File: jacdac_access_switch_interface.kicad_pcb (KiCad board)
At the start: 2 copper layers, 25 x 35 mm, 26 parts, among them J1 Conn_Jacdac_CardEdge, J2 Conn_HackConnect, J3 jack_3.5_pj313d, J4 jack_3.5_pj313d, U1 NCP114ASN330T1G, U2 STM32G031J6M6, U3 AQY282, U4 AQY282

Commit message: Setting up v1.5, combined input-output
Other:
- board text added: "Switch interface v1.5"
- board text removed: "Switch output v1.4"
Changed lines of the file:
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@@
   (paper "A4")
   (title_block
-    (title "Jacdac access switch output")
+    (title "Jacdac access switch interface")
     (date "2022-01-07")
-    (rev "v1.4")
+    (rev "v1.5")
     (comment 3 "Matthew Oppenheim")
     (comment 4 "Licence: Attribution 4.0 International (CC BY 4.0)")
@@
   (gr_rect (start 154.5 67.5) (end 167.5 69)
     (stroke (width 0.05) (type default)) (fill none) (layer "F.CrtYd"))
-  (gr_text "Switch output\nv1.4" (at 162.5 110.5) (layer "B.SilkS")
+  (gr_text "Switch interface\nv1.5" (at 162.5 110.5) (layer "B.SilkS")
     (effects (font (size 1 1) (thickness 0.16)) (justify mirror))
   )

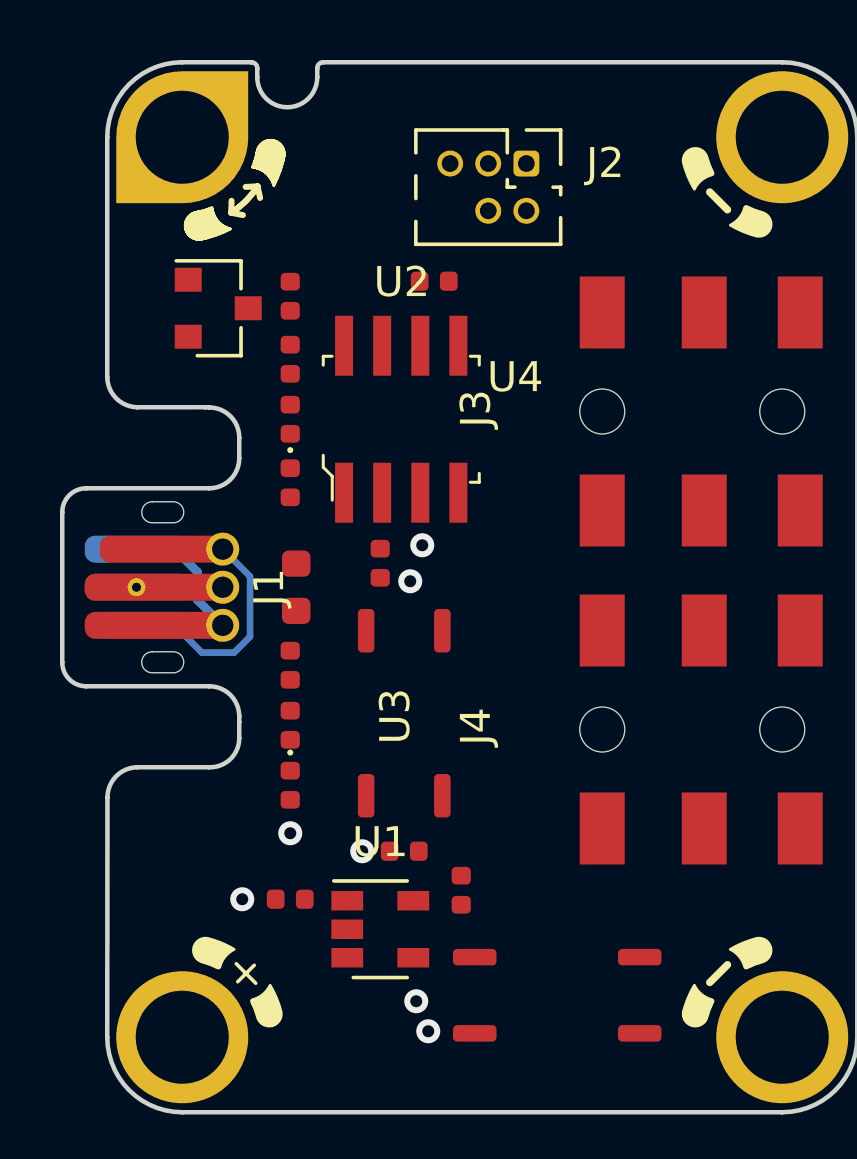
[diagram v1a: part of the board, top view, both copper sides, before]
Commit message: Moving footprint text from silkscreen to user comments
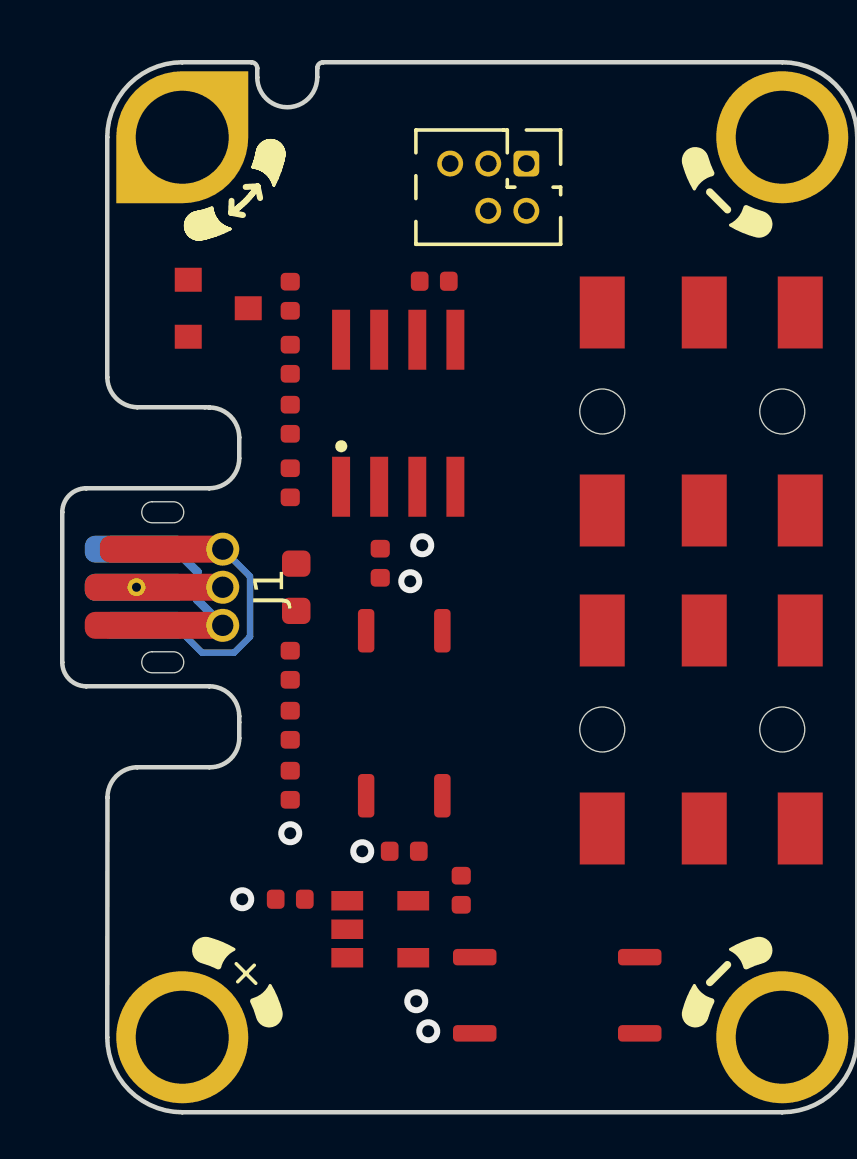
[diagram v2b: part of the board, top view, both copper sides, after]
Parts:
- moved U2 0.22 mm to (157.2, 79.2)

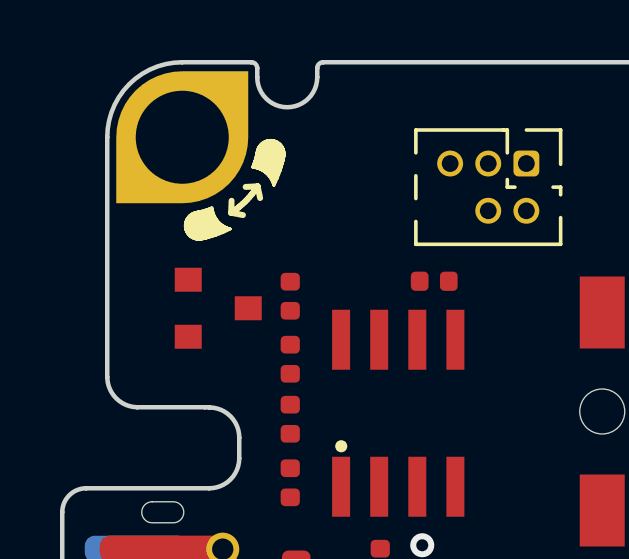
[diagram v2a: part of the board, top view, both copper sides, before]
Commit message: Added input protection. Changed MCU to 20 pin STM32G031F6P6
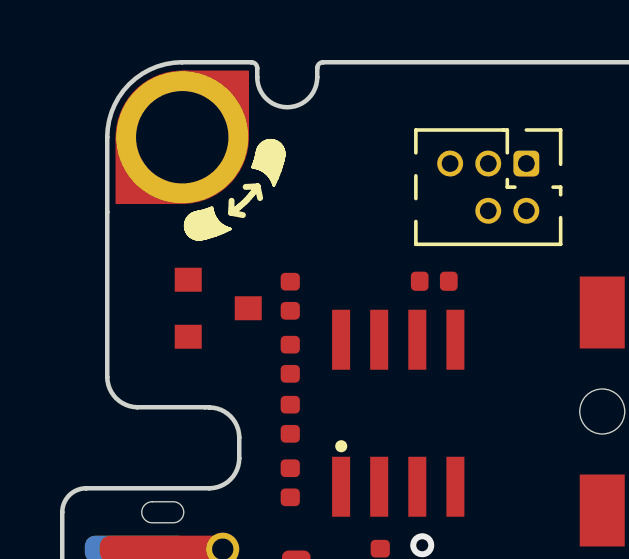
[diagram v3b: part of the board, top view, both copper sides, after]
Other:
- outline, holes or cut-outs redrawn

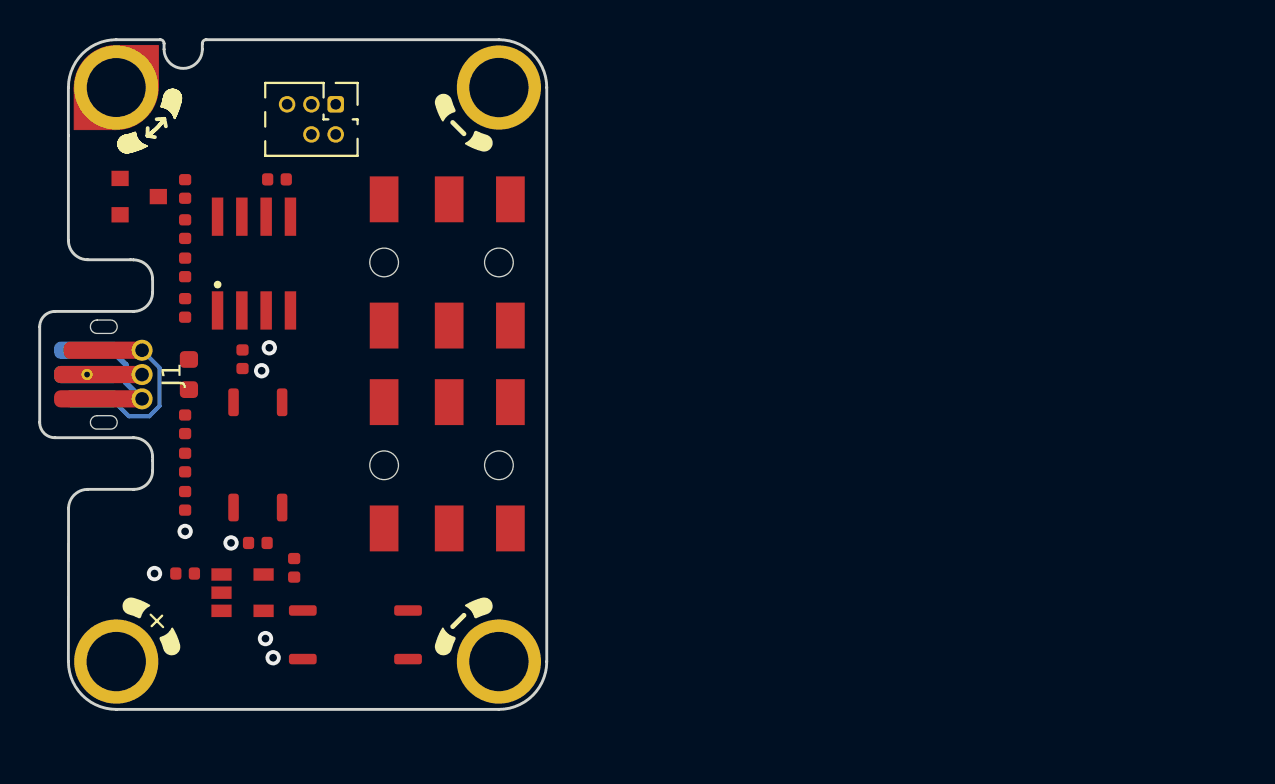
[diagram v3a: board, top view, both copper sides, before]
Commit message: Replaced opto-isoltated relays with discrete FET relays
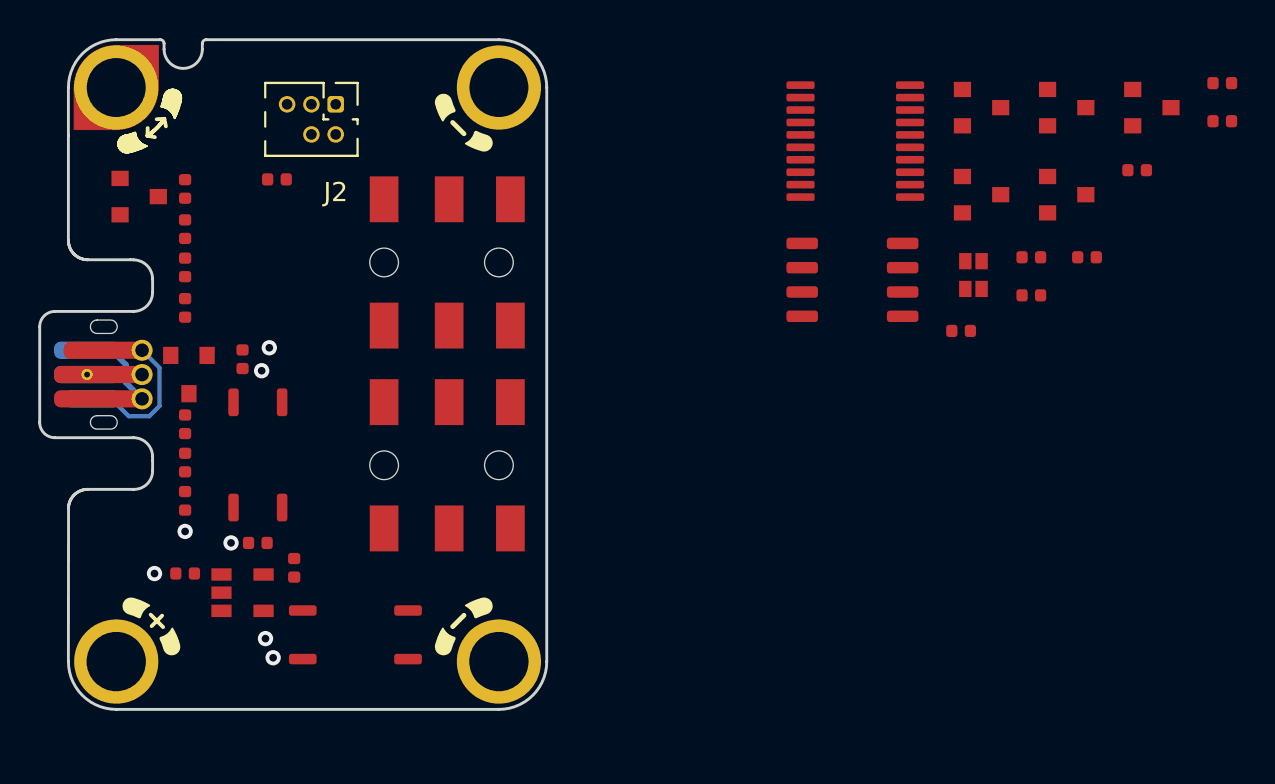
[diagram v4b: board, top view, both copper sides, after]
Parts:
- removed U2: STM32G031J6M6, jacdac_access_switch_interface:SOIC-8_W3.9mm
- added D10: BAT54S, jacdac_access_switch_interface:SOT-23, F.Cu at (199.7, 75.6)
- added D5: LTST-C19HE1WT, jacdac_access_switch_interface:LED_LTST-C19HE1WT, F.Cu at (194.8, 79.8)
- added D6: BAT54S, jacdac_access_switch_interface:SOT-23, F.Cu at (204.1, 71.0)
- added D7: BAT54S, jacdac_access_switch_interface:SOT-23, F.Cu at (199.7, 71.0)
- added D8: BAT54S, jacdac_access_switch_interface:SOT-23, F.Cu at (195.2, 71.0)
- added D9: BAT54S, jacdac_access_switch_interface:SOT-23, F.Cu at (195.2, 75.6)
- added Q1: WSP6946, jacdac_access_switch_interface:SOP-8_3.9x4.9mm_P1.27mm, F.Cu at (188.5, 80.0)
- added R10: 100K, jacdac_access_switch_interface:R_0402_1005Metric, F.Cu at (207.8, 71.8)
- added R11: 100K, jacdac_access_switch_interface:R_0402_1005Metric, F.Cu at (200.7, 78.9)
- added R12: 100K, jacdac_access_switch_interface:R_0402_1005Metric, F.Cu at (194.2, 82.7)
- added R6: 150, jacdac_access_switch_interface:R_0402_1005Metric, F.Cu at (197.8, 80.9)
- added R7: 33, jacdac_access_switch_interface:R_0402_1005Metric, F.Cu at (203.4, 74.3)
- added R8: 33, jacdac_access_switch_interface:R_0402_1005Metric, F.Cu at (207.8, 69.8)
- added R9: 100K, jacdac_access_switch_interface:R_0402_1005Metric, F.Cu at (197.8, 78.9)
- added U5: STM32G031F6P6, jacdac_access_switch_interface:TSSOP-20_4.4x6.5mm_P0.65mm, F.Cu at (188.6, 72.8)
- D4: value LED -> BAT54S; footprint jacdac_access_switch_interface:LED_0603_1608Metric -> jacdac_access_switch_interface:SOT-23
- R4: value 330 -> 100K
- R5: value 220 -> 100K
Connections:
- net /PLUG_TIP1 renamed /TIP1
- net /PLUG_TIP2 renamed /TIP2
- D3 pad 3: /JD_DATA_MCU_SWCLK -> Net-(D3-common)
- D4 pad 1: /JD_STATUS -> GND
- D4 pad 2: Net-(D4-A) -> +3V3
- J2 pad 4: /JD_DATA_MCU_SWCLK -> /SWDCLK
- J3 pad 3: /SLEEVE1 -> /RING1
- J4 pad 3: /SLEEVE2 -> /RING2
- R1 pad 1: /JD_DATA_MCU_SWCLK -> Net-(D3-common)
- R2 pad 2: /SWITCH1 -> /RELAY1
- R3 pad 2: /SWITCH2 -> /RELAY2
- R4 pad 1: +3V3 -> /SLEEVE1_P
- R4 pad 2: Net-(D4-A) -> unconnected-(R4-Pad2)
- R5 pad 1: +3V3 -> /RING1_P
- R5 pad 2: Net-(D4-A) -> unconnected-(R5-Pad2)
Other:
- board text added: "Switch interface v1.6"
- board text removed: "Switch interface v1.5"

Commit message: Initial component placement for PCB
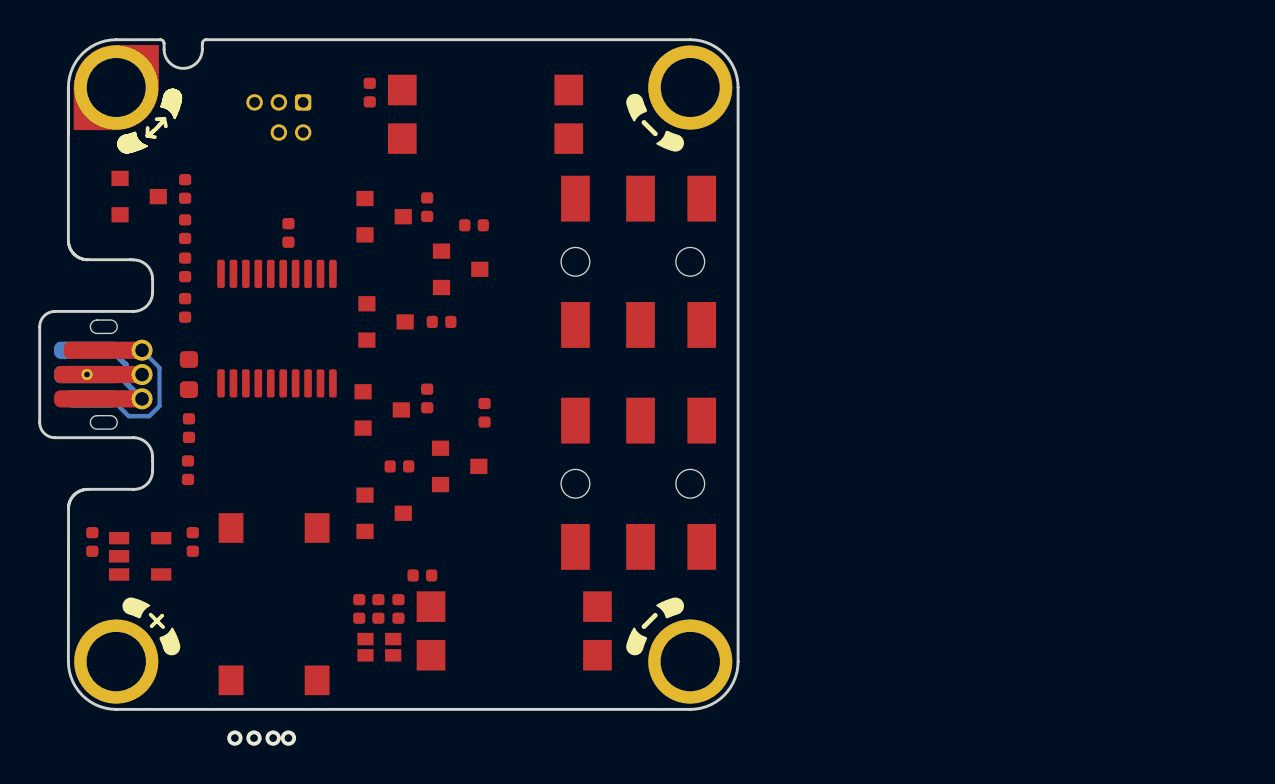
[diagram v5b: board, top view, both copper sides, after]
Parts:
- removed Q1: WSP6946, jacdac_access_switch_interface:SOP-8_3.9x4.9mm_P1.27mm
- removed U5: STM32G031F6P6, jacdac_access_switch_interface:TSSOP-20_4.4x6.5mm_P0.65mm
- added D12: LED_status, jacdac_access_switch_interface:LED_0603_1608Metric, F.Cu at (153.8, 85.0)
- added R13: 130, jacdac_access_switch_interface:R_0402_1005Metric, F.Cu at (153.8, 87.8)
- added SW1: SW_PT645SM43SMTR92LFS, jacdac_access_switch_interface:SW_SPST_PTS645, F.Cu at (158.2, 97.0)
- added U2: STM32G030F6P6, jacdac_access_switch_interface:TSSOP-20_4.4x6.5mm_P0.65mm, F.Cu at (158.4, 82.6)
- R10, R11, R12, R4, R5, R9: value 100K -> 10K
- U3, U4: value AQY282 -> TLP240A; footprint jacdac_access_switch_interface:SOP-4_3.8x4.1mm_P2.54mm -> jacdac_access_switch_interface:TLP240A_TP1_LF1
- moved R8 51.1 mm to (164.8, 97.2), turned to 90 degrees
- moved R7 45.8 mm to (163.7, 97.2), turned to 90 degrees
- moved R10 44.0 mm to (166.2, 86.2), turned to -90 degrees
- moved D10 39.4 mm to (164.0, 92.2)
- moved R6 38.8 mm to (162.7, 97.2), turned to 90 degrees
- moved D7 37.3 mm to (164.1, 82.2)
- moved D6 37.1 mm to (168.0, 79.5)
- moved D5 36.6 mm to (163.8, 99.2), turned to 90 degrees
- moved D8 35.1 mm to (163.9, 86.8)
- moved R11 32.5 mm to (169.2, 87.0), turned to -90 degrees
- moved R9 31.0 mm to (167.0, 82.2), turned to 180 degrees
- moved D9 30.8 mm to (167.9, 89.8)
- moved R12 30.2 mm to (164.8, 89.8)
- moved U4 27.9 mm to (169.2, 71.5)
- moved R3 25.1 mm to (163.2, 70.3), turned to -90 degrees
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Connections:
- D10 pad 3: /TIP2 -> /TIP2_P
- D4 pad 3: /SLEEVE1 -> /SLEEVE1_P
- D5 pad 4: unconnected-(D5-Pad4) -> +3V3
- D6 pad 3: /RING1 -> /RING1_P
- D7 pad 3: /TIP1 -> /TIP1_P
- D8 pad 3: /SLEEVE2 -> /SLEEVE2_P
- D9 pad 3: /RING2 -> /RING2_P
- MH1 pad MH1: /JD_DATA_MCU_SWCLK -> /JD_DATA
- R10 pad 1: /SLEEVE2_P -> /SLEEVE2
- R10 pad 2: unconnected-(R10-Pad2) -> /SLEEVE2_P
- R11 pad 1: /RING2_P -> /RING2
- R11 pad 2: unconnected-(R11-Pad2) -> /RING2_P
- R12 pad 1: /TIP2_P -> /TIP2
- R12 pad 2: unconnected-(R12-Pad2) -> /TIP2_P
- R2 pad 2: /RELAY1 -> /RELAY2
- R3 pad 2: /RELAY2 -> /RELAY1
- R4 pad 1: /SLEEVE1_P -> /SLEEVE1
- R4 pad 2: unconnected-(R4-Pad2) -> /SLEEVE1_P
- R5 pad 1: /RING1_P -> /RING1
- R5 pad 2: unconnected-(R5-Pad2) -> /RING1_P
- R9 pad 1: /TIP1_P -> /TIP1
- R9 pad 2: unconnected-(R9-Pad2) -> /TIP1_P
- U3 pad 3: /SLEEVE1 -> /SLEEVE2
- U3 pad 4: /TIP1 -> /TIP2
- U4 pad 3: /SLEEVE2 -> /SLEEVE1
- U4 pad 4: /TIP2 -> /TIP1
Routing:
- net GND: vias 7 -> 4
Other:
- board size 25 x 35 mm -> 35 x 35 mm
- board text added: "Access switch interface v1.7 mattoppenheim.com"
- board text removed: "Switch interface v1.6"

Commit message: Updated footprint identifiers, routing started
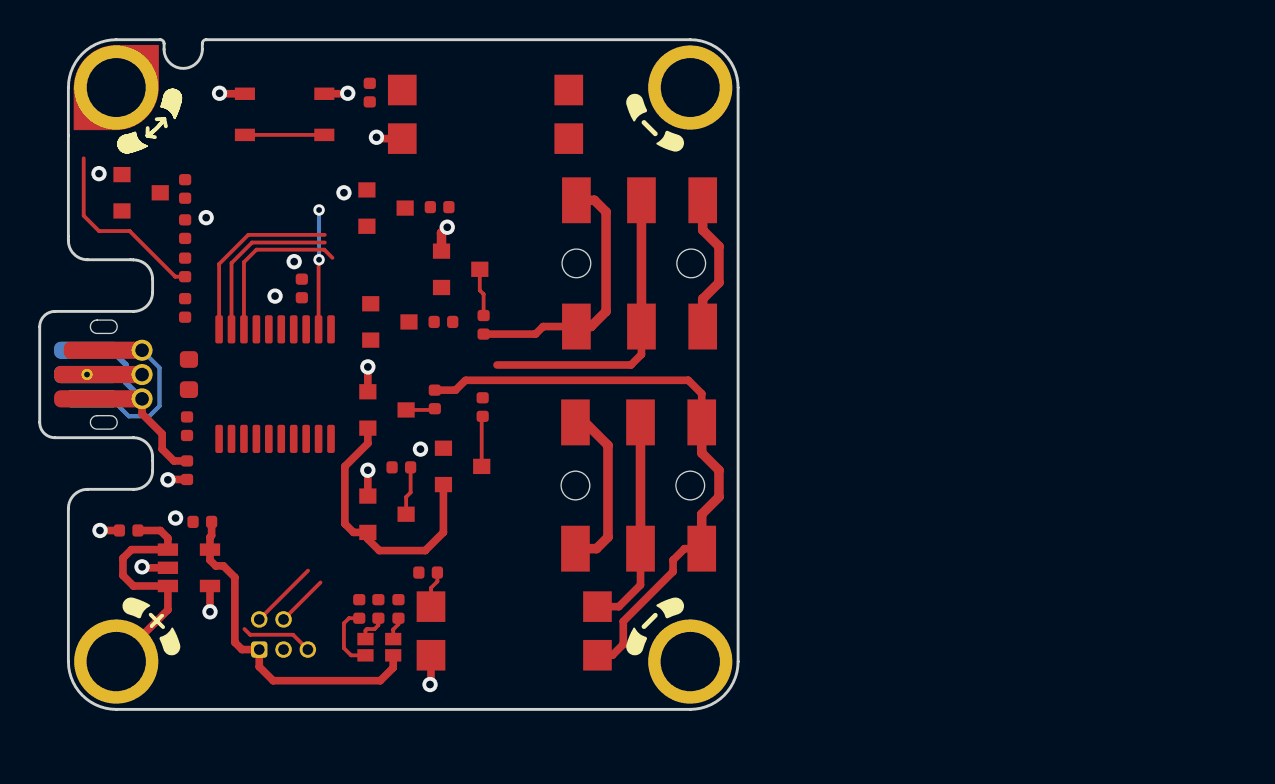
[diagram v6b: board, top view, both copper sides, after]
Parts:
- SW1: value SW_PT645SM43SMTR92LFS -> SW_PTS810; footprint jacdac_access_switch_interface:SW_SPST_PTS645 -> jacdac_access_switch_interface:SW_SPST_PTS810
- moved J2 27.1 mm to (158.8, 98.6), turned to 180 degrees
- moved SW1 25.6 mm to (158.8, 71.4), turned to 0 degrees
- moved R5 5.22 mm to (169.2, 82.4), turned to 90 degrees
- moved J4 3.57 mm to (177.2, 90.8)
- moved J3 3.54 mm to (177.2, 79.2)
- moved C4 2.98 mm to (159.7, 80.5)
- moved U2 2.90 mm to (158.3, 85.5)
- moved U1 2.62 mm to (153.8, 95.1)
- moved C1 1.99 mm to (150.7, 93.2), turned to 180 degrees
- moved C2 1.16 mm to (154.5, 92.7), turned to 180 degrees
- moved R4 0.65 mm to (166.9, 76.2), turned to 180 degrees
- moved D4 0.46 mm to (164.1, 76.3)
- moved R10 0.40 mm to (166.7, 86.3)
- moved R2 0.34 mm to (166.3, 95.3)
- moved R11 0.32 mm to (169.2, 86.7)
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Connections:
- SW1 pad 1: /nFLASH -> GND
- SW1 pad 2: GND -> /nFLASH
- U2 pad 10: /TIP1_P -> /SLEEVE1_P
- U2 pad 8: /SLEEVE1_P -> /TIP1_P
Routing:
- net /SLEEVE2: track 0.00 -> 32.1 mm
- net +3V3: track 0.00 -> 32.0 mm
- net JD_PWR: track 0.00 -> 18.0 mm
- net /TIP1: track 0.00 -> 15.8 mm
- net GND: track 0.00 -> 14.3 mm, vias 4 -> 18
- net /RING1: track 0.00 -> 13.9 mm
- net /RING1_P: track 0.00 -> 11.3 mm
- net /TIP2: track 0.00 -> 11.2 mm
- net /nFLASH: track 0.00 -> 10.5 mm, vias 0 -> 2
- net /JD_DATA: track 0.00 -> 9.62 mm
- net /SLEEVE1_P: track 0.00 -> 9.57 mm
- net /RING2: track 0.00 -> 8.95 mm
- net /TIP1_P: track 0.00 -> 8.58 mm
- net /SLEEVE1: track 0.00 -> 7.30 mm
- net /nRESET: track 0.00 -> 3.76 mm
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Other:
- outline, holes or cut-outs redrawn
